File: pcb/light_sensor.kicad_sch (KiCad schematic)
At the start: 3 parts, among them J7 Screw_Terminal_01x03

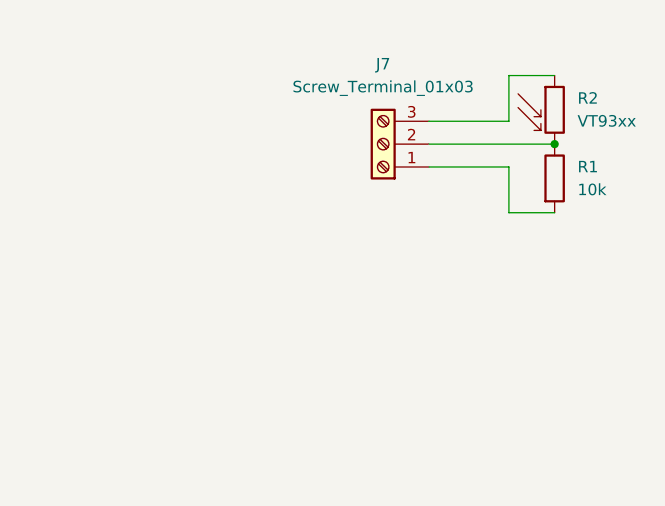
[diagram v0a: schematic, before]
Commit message: redesigning the circuit of the rellay and starting to adjust the footprints
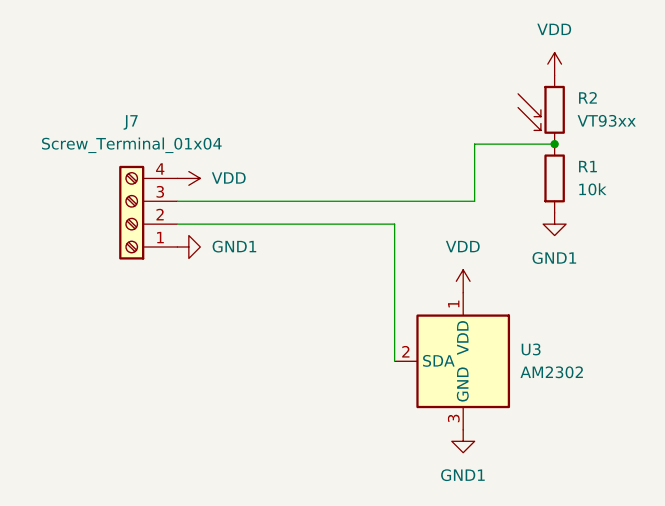
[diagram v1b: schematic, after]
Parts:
- removed J7: Screw_Terminal_01x03, symbol Connector:Screw_Terminal_01x03
- added J7: Screw_Terminal_01x04, symbol Connector:Screw_Terminal_01x04
- added U3: AM2302, Sensor:ASAIR_AM2302_P2.54mm_Vertical, symbol Sensor:AM2302
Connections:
- net GND1: now reaches R1.2
- net GND1: now also J7.1 (Pin_1), U3.3 (GND), U3.4 (GND)
- net at R1.1, R2.2: now also J7.3 (Pin_3)
- net VDD: now reaches R2.1
- net VDD: now also J7.4 (Pin_4), U3.1 (VDD)
- new net: J7.2 (Pin_2), U3.2 (SDA)

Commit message: finishing the bom and adding the jlc number of the parts
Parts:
- J7: footprint (none) -> TerminalBlock_Phoenix:TerminalBlock_Phoenix_MKDS-1,5-4_1x04_P5.00mm_Horizontal; jlc part # (none) -> C90087
- R1: footprint (none) -> Resistor_SMD:R_0603_1608Metric_Pad0.98x0.95mm_HandSolder; amazon link (none) -> https://www.amazon.com/100PCS-0603-SMD-chip-resistors/dp/B0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; jlc part # (none) -> C15401
- R2: amazon link (none) -> https://www.amazon.com/eBoot-Photoresistor-Sensitive-Resist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; jlc part # (none) -> C10077
- U3: jlc part # (none) -> C83988
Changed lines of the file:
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@@
+			)
+		)
+		(property "jlc part #" "C83988"
+			(at 104.14 124.46 0)
+			(effects
+				(font
+					(size 1.27 1.27)
+				)
+				(hide yes)
 			)
 		)
@@
 			)
 		)
-		(property "amazon link" ""
+		(property "amazon link" "https://www.amazon.com/eBoot-Photoresistor-Sensitive-Resistor-Dependent/dp/B01N7V536K?"
+			(at 114.3 96.52 0)
+			(effects
+				(font
+					(size 1.27 1.27)
+				)
+				(hide yes)
+			)
+		)
+		(property "jlc part #" "C10077"
 			(at 114.3 96.52 0)
 			(effects
@@
 			)
 		)
-		(property "Footprint" ""
+		(property "Footprint" "Resistor_SMD:R_0603_1608Metric_Pad0.98x0.95mm_HandSolder"
 			(at 112.522 104.14 90)
 			(effects
@@
 			)
 		)
-		(property "amazon link" ""
+		(property "amazon link" "https://www.amazon.com/100PCS-0603-SMD-chip-resistors/dp/B0B3SY4DCP?"
+			(at 114.3 104.14 0)
+			(effects
+				(font
+					(size 1.27 1.27)
+				)
+				(hide yes)
+			)
+		)
+		(property "jlc part #" "C15401"
 			(at 114.3 104.14 0)
 			(effects
@@
 			)
 		)
-		(property "Footprint" ""
+		(property "Footprint" "TerminalBlock_Phoenix:TerminalBlock_Phoenix_MKDS-1,5-4_1x04_P5.00mm_Horizontal"
 			(at 67.31 109.22 0)
 			(effects
@@
 			(at 67.31 109.22 0)
 			(effects
+				(font
+					(size 1.27 1.27)
+				)
+				(hide yes)
+			)
+		)
+		(property "jlc part #" "C90087"
+			(at 67.31 109.22 0)
+			(effects

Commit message: polishing the pcb
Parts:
- U3: footprint Sensor:ASAIR_AM2302_P2.54mm_Vertical -> Sensor:ASAIR_AM2302_P2.54mm_Lead2.75mm_TabDown
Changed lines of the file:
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@@
 			)
 		)
-		(property "Footprint" "Sensor:ASAIR_AM2302_P2.54mm_Vertical"
+		(property "Footprint" "Sensor:ASAIR_AM2302_P2.54mm_Lead2.75mm_TabDown"
 			(at 104.14 134.62 0)
 			(effects

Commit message: fixing the layout
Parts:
- R1: amazon link https://www.amazon.com/100PCS-0603-SMD-chip-resistors/dp/B0B3SY4DCP? -> https://www.amazon.com/100PCS-0603-SMD-chip-resistors/dp/B0B3SY4DCP? https://www.amazon.com/100PCS-0603-SMD-chip-resistors/dp/B0B3SY4DCP?; jlc part # C15401 -> C2906982
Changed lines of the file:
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@@
 			)
 		)
-		(property "amazon link" "https://www.amazon.com/100PCS-0603-SMD-chip-resistors/dp/B0B3SY4DCP?"
+		(property "amazon link" "https://www.amazon.com/100PCS-0603-SMD-chip-resistors/dp/B0B3SY4DCP? https://www.amazon.com/100PCS-0603-SMD-chip-resistors/dp/B0B3SY4DCP?"
 			(at 114.3 104.14 0)
 			(effects
@@
 			)
 		)
-		(property "jlc part #" "C15401"
+		(property "jlc part #" "C2906982"
 			(at 114.3 104.14 0)
 			(effects

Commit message: Finishing the carrier board with the new usb-c modul
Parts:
- renumbered J7 to J10, R2 to R4, R1 to R5
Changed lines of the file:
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@@
 		(dnp no)
 		(fields_autoplaced yes)
-		(property "Reference" "#PWR023"
+		(property "Reference" "#PWR027"
 			(at 114.3 96.52 0)
 			(hide yes)
@@
 			(project "pcb"
 				(path "/2955ee96-3683-4cf6-bfa3-83b5e4980920/f55e4a84-be84-408f-9efd-18451ab0cbe4"
-					(reference "#PWR023")
+					(reference "#PWR027")
 					(unit 1)
 				)
@@
 		(dnp no)
 		(fields_autoplaced yes)
-		(property "Reference" "#PWR022"
+		(property "Reference" "#PWR025"
 			(at 104.14 120.65 0)
 			(hide yes)
@@
 			(project "pcb"
 				(path "/2955ee96-3683-4cf6-bfa3-83b5e4980920/f55e4a84-be84-408f-9efd-18451ab0cbe4"
-					(reference "#PWR022")
+					(reference "#PWR025")
 					(unit 1)
 				)
@@
 		(dnp no)
 		(fields_autoplaced yes)
-		(property "Reference" "R2"
+		(property "Reference" "R4"
 			(at 116.84 95.2499 0)
 			(show_name no)
@@
 			(project "pcb"
 				(path "/2955ee96-3683-4cf6-bfa3-83b5e4980920/f55e4a84-be84-408f-9efd-18451ab0cbe4"
-					(reference "R2")
+					(reference "R4")
 					(unit 1)
 				)
@@
 		(dnp no)
 		(fields_autoplaced yes)
-		(property "Reference" "#PWR025"
+		(property "Reference" "#PWR028"
 			(at 114.3 114.3 0)
 			(hide yes)
@@
 			(project "pcb"
 				(path "/2955ee96-3683-4cf6-bfa3-83b5e4980920/f55e4a84-be84-408f-9efd-18451ab0cbe4"
-					(reference "#PWR025")
+					(reference "#PWR028")
 					(unit 1)
 				)
@@
 		(dnp no)
 		(fields_autoplaced yes)
-		(property "Reference" "R1"
+		(property "Reference" "R5"
 			(at 116.84 102.8699 0)
 			(show_name no)
@@
 			(project "pcb"
 				(path "/2955ee96-3683-4cf6-bfa3-83b5e4980920/f55e4a84-be84-408f-9efd-18451ab0cbe4"
-					(reference "R1")
+					(reference "R5")
 					(unit 1)
 				)
@@
 		(dnp no)
 		(fields_autoplaced yes)
-		(property "Reference" "#PWR018"
+		(property "Reference" "#PWR024"
 			(at 78.74 111.76 0)
 			(hide yes)
@@
 			(project "pcb"
 				(path "/2955ee96-3683-4cf6-bfa3-83b5e4980920/f55e4a84-be84-408f-9efd-18451ab0cbe4"
-					(reference "#PWR018")
+					(reference "#PWR024")
 					(unit 1)
 				)
@@
 		(dnp no)
 		(fields_autoplaced yes)
-		(property "Reference" "J7"
+		(property "Reference" "J10"
 			(at 67.31 97.79 0)
 			(show_name no)
@@
 			(project "pcb"
 				(path "/2955ee96-3683-4cf6-bfa3-83b5e4980920/f55e4a84-be84-408f-9efd-18451ab0cbe4"
-					(reference "J7")
+					(reference "J10")
 					(unit 1)
 				)
@@
 		(dnp no)
 		(fields_autoplaced yes)
-		(property "Reference" "#PWR024"
+		(property "Reference" "#PWR023"
 			(at 68.58 104.14 0)
 			(hide yes)
@@
 			(project "pcb"
 				(path "/2955ee96-3683-4cf6-bfa3-83b5e4980920/f55e4a84-be84-408f-9efd-18451ab0cbe4"
-					(reference "#PWR024")
-					(unit 1)
-				)
+					(reference "#PWR023")
+					(unit 1)
+				)
